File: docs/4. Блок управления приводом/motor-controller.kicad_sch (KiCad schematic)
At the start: 13 parts, among them J1 Raspberry_Pi_4, J2 Conn_01x02_Pin, J3 Conn_01x02_Pin, M1 Motor_DC, M2 Motor_DC, SW1 SW_SPST, SW2 RotaryEncoder, SW3 RotaryEncoder, U1 L298N, U2 PCA9306

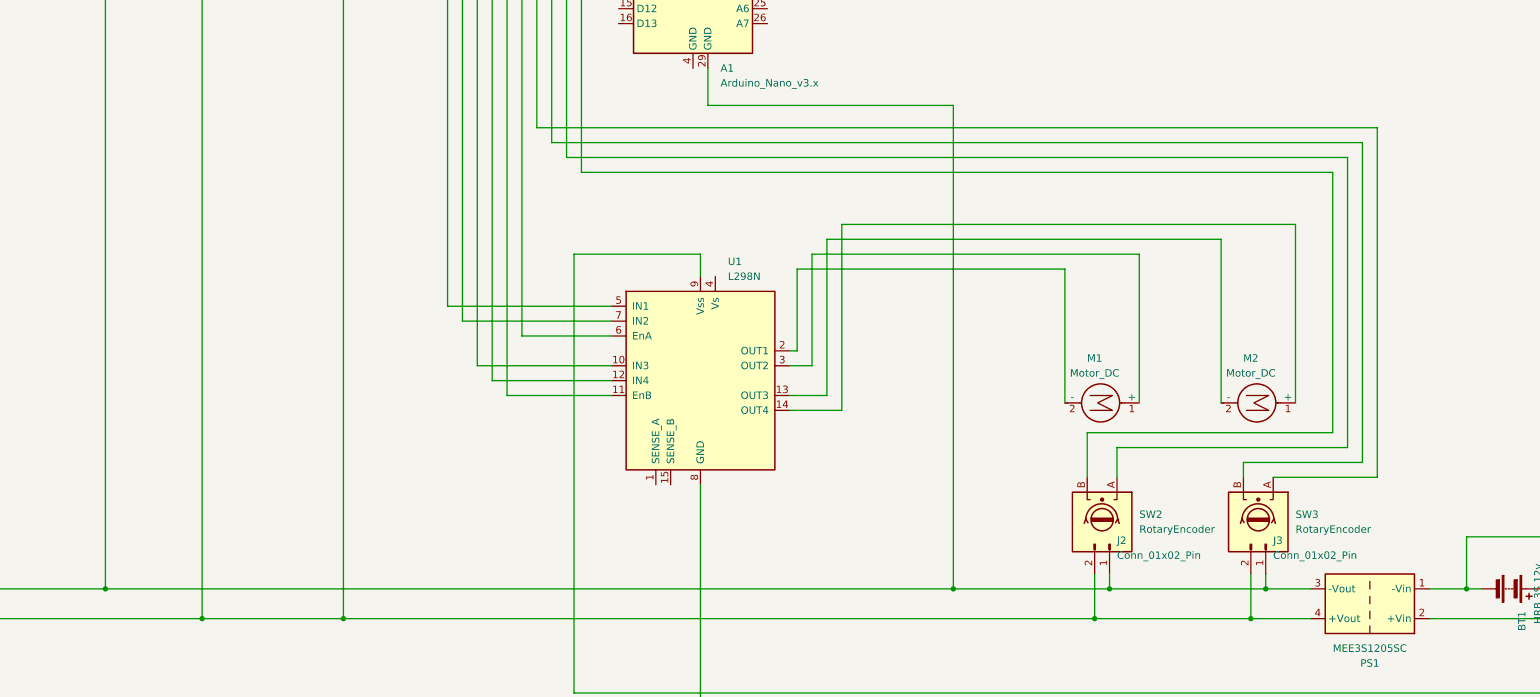
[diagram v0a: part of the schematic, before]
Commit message: Реализован метод speed. Бот едет почти прямо.
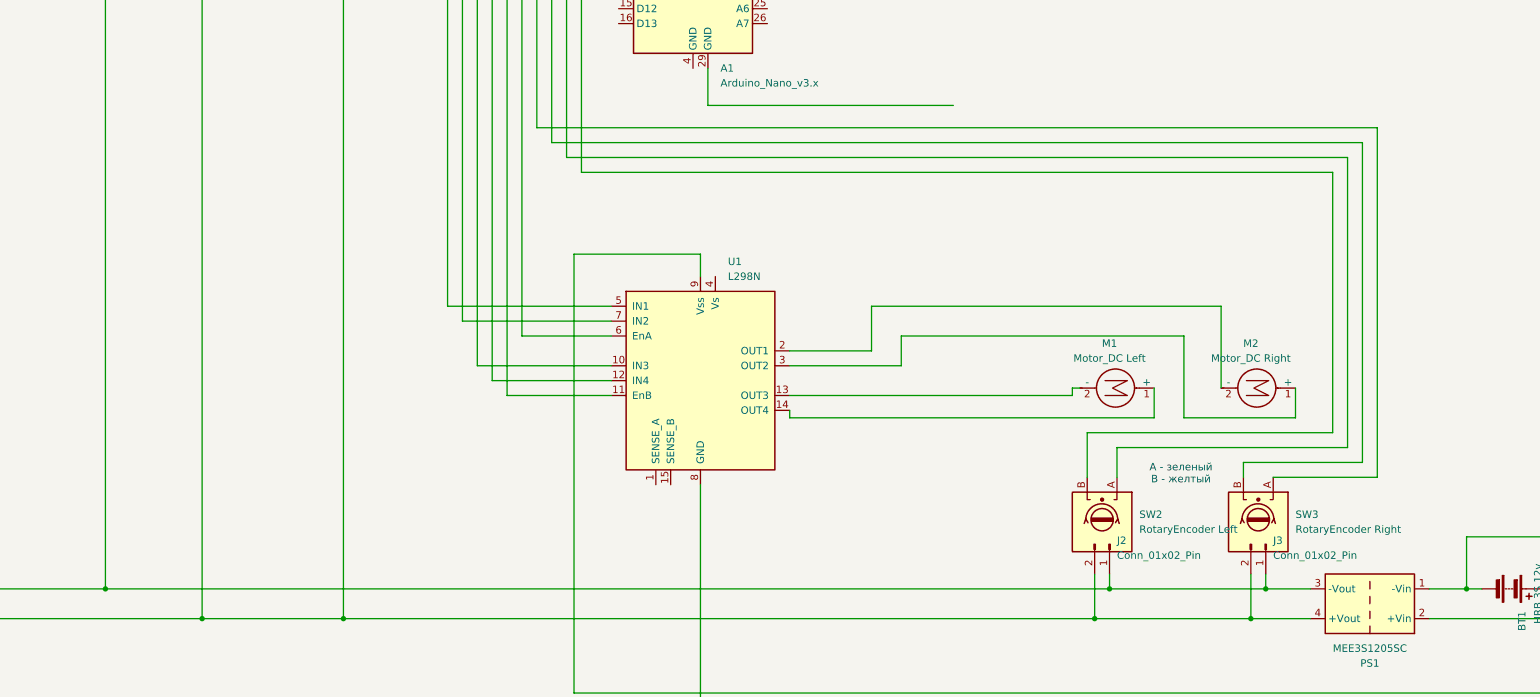
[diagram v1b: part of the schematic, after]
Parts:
- M1: value Motor_DC -> Motor_DC Left
- M2: value Motor_DC -> Motor_DC Right
- SW2: value RotaryEncoder -> RotaryEncoder Left
- SW3: value RotaryEncoder -> RotaryEncoder Right
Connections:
- net at U1.13 (OUT3): now also M1.2 (-); no longer M2.2 (-)
- net at U1.14 (OUT4): now also M1.1 (+); no longer M2.1 (+)
- net at U1.2 (OUT1): now also M2.2 (-); no longer M1.2 (-)
- net at U1.3 (OUT2): now also M2.1 (+); no longer M1.1 (+)
- net at J1.14 (GND), J1.20 (GND), J1.25 (GND)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: no longer A1.29 (GND)
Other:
- note added: "А - зеленый B - желтый"
- moved on the sheet: M1, M2

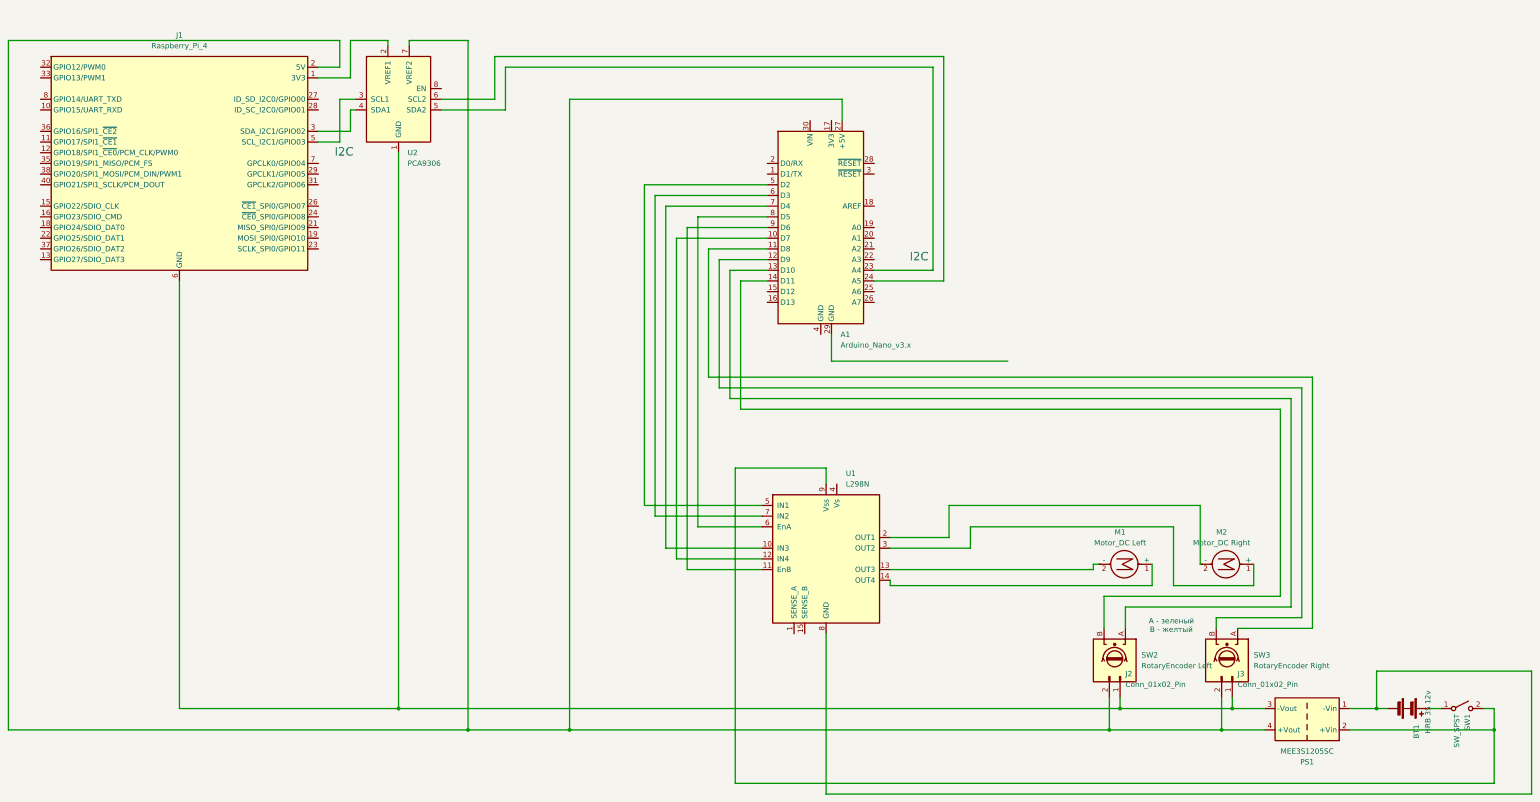
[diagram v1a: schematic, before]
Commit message: Энкодеры перенесены на отдельный порт с аппаратным прерыванием
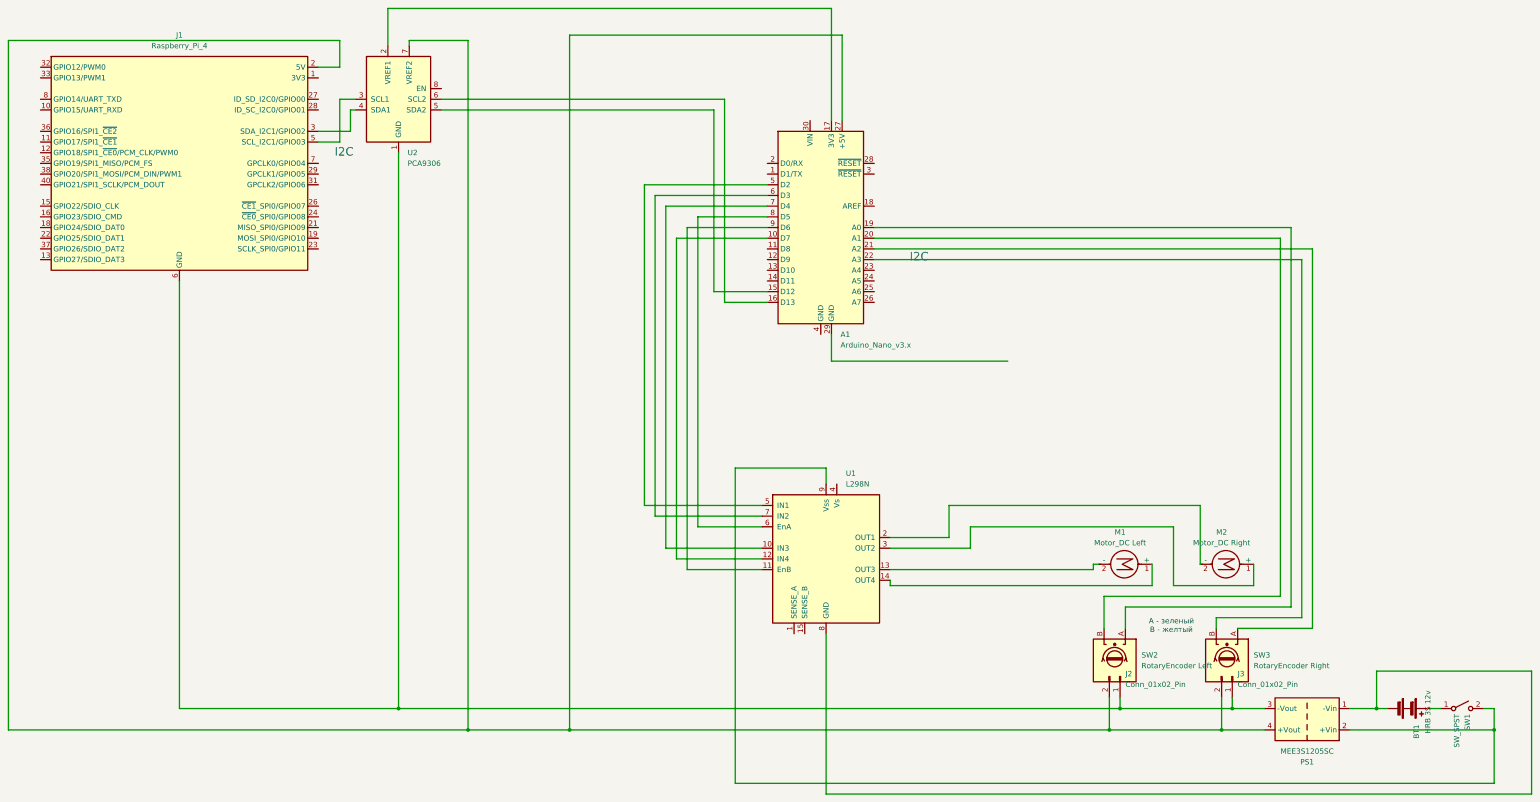
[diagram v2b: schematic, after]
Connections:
- net at SW3.A: now also A1.21 (A2); no longer A1.11 (D8)
- net at SW3.B: now also A1.22 (A3); no longer A1.12 (D9)
- net at J1.1 (3V3), J1.17 (3V3): no longer U2.2 (VREF1)
- net at U2.5 (SDA2): now also A1.15 (D12); no longer A1.23 (A4)
- net at U2.6 (SCL2): now also A1.16 (D13); no longer A1.24 (A5)
- net at SW2.A: now also A1.19 (A0); no longer A1.13 (D10)
- net at SW2.B: now also A1.20 (A1); no longer A1.14 (D11)
- net at A1.17 (3V3): now also U2.2 (VREF1)
